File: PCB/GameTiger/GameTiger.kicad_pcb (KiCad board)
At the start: 2 copper layers, 5 parts, among them U1 RP2040, U2 NCP1117-3.3_SOT223, U3 W25Q128JVS, U4 PAM8302A, U5 PCF8575DB

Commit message: PCB Schematic for V2.0 is completed
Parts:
- added D1: MBR0540, Diode_SMD:D_SOD-123, F.Cu at (156.7, 83.3)
- U2: value NCP1117-3.3_SOT223 -> MCP73831-2-OT; footprint Package_TO_SOT_SMD:SOT-223-3_TabPin2 -> Package_TO_SOT_SMD:SOT-23-5
- U5: value PCF8575DB -> AP2112K-3.3; footprint PCF8575:pcf8575dbr -> Package_TO_SOT_SMD:SOT-23-5
- moved U4 21.3 mm to (109.6, 96.3)
- moved U5 7.34 mm to (144.2, 68.0)
- turned U2 to -90 degrees
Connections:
- net Net-(J2-CLK) renamed MicroSD_CLK
- net Net-(J2-CMD) renamed MicroSD_MOSI
- net Net-(J2-DAT0) renamed MicroSD_MISO
- net Net-(J2-DAT3/CD) renamed MicroSD_CS
- net Net-(U1-QSPI_SCLK) renamed Flash_QSPI_CLK
- net Net-(U1-QSPI_SD0) renamed Flash_QSPI_SD0
- net Net-(U1-QSPI_SD1) renamed Flash_QSPI_SD1
- net Net-(U1-QSPI_SD2) renamed Flash_QSPI_SD2
- net Net-(U1-QSPI_SD3) renamed Flash_QSPI_SD3
- net Net-(U1-QSPI_SS) renamed Flash_QSPI_SS
- net Net-(U1-XIN) renamed Crystal_XIN
- U1 pad 11: unconnected-(U1-GPIO8-Pad11) -> LCD_DC
- U1 pad 12: unconnected-(U1-GPIO9-Pad12) -> LCD_CS
- U1 pad 13: unconnected-(U1-GPIO10-Pad13) -> LCD_CLK
- U1 pad 14: unconnected-(U1-GPIO11-Pad14) -> LCD_DATA
- U1 pad 15: unconnected-(U1-GPIO12-Pad15) -> KYBD_UP
- U1 pad 16: unconnected-(U1-GPIO13-Pad16) -> KYBD_DOWN
- U1 pad 17: unconnected-(U1-GPIO14-Pad17) -> KYBD_LEFT
- U1 pad 18: unconnected-(U1-GPIO15-Pad18) -> KYBD_RIGHT
- U1 pad 2: Net-(U1-GPIO0) -> unconnected-(U1-GPIO0-Pad2)
- U1 pad 26: unconnected-(U1-RUN-Pad26) -> Net-(U1-RUN)
- U1 pad 27: unconnected-(U1-GPIO16-Pad27) -> KYBD_A
- U1 pad 28: unconnected-(U1-GPIO17-Pad28) -> KYBD_B
- U1 pad 29: unconnected-(U1-GPIO18-Pad29) -> KYBD_SELECT
- U1 pad 30: unconnected-(U1-GPIO19-Pad30) -> KYBD_START
- U1 pad 31: Net-(U1-GPIO20) -> Audio_PWM
- U1 pad 32: Net-(U1-GPIO21) -> MicroSD_DET
- U1 pad 9: unconnected-(U1-GPIO7-Pad9) -> LCD_RESET
- U2 pad 1: GND -> Net-(U2-STAT)
- U2 pad 2: +3.3V -> GND
- U2 pad 3: VBUS -> VBAT
- U4 pad 6: +3.3V -> VBAT
- U5 pad 1: unconnected-(U5-*INT-Pad1) -> Net-(D1-K)
- U5 pad 2: unconnected-(U5-A1-Pad2) -> GND
- U5 pad 3: unconnected-(U5-A2-Pad3) -> Net-(U5-EN)
- U5 pad 5: unconnected-(U5-P01-Pad5) -> +3.3V

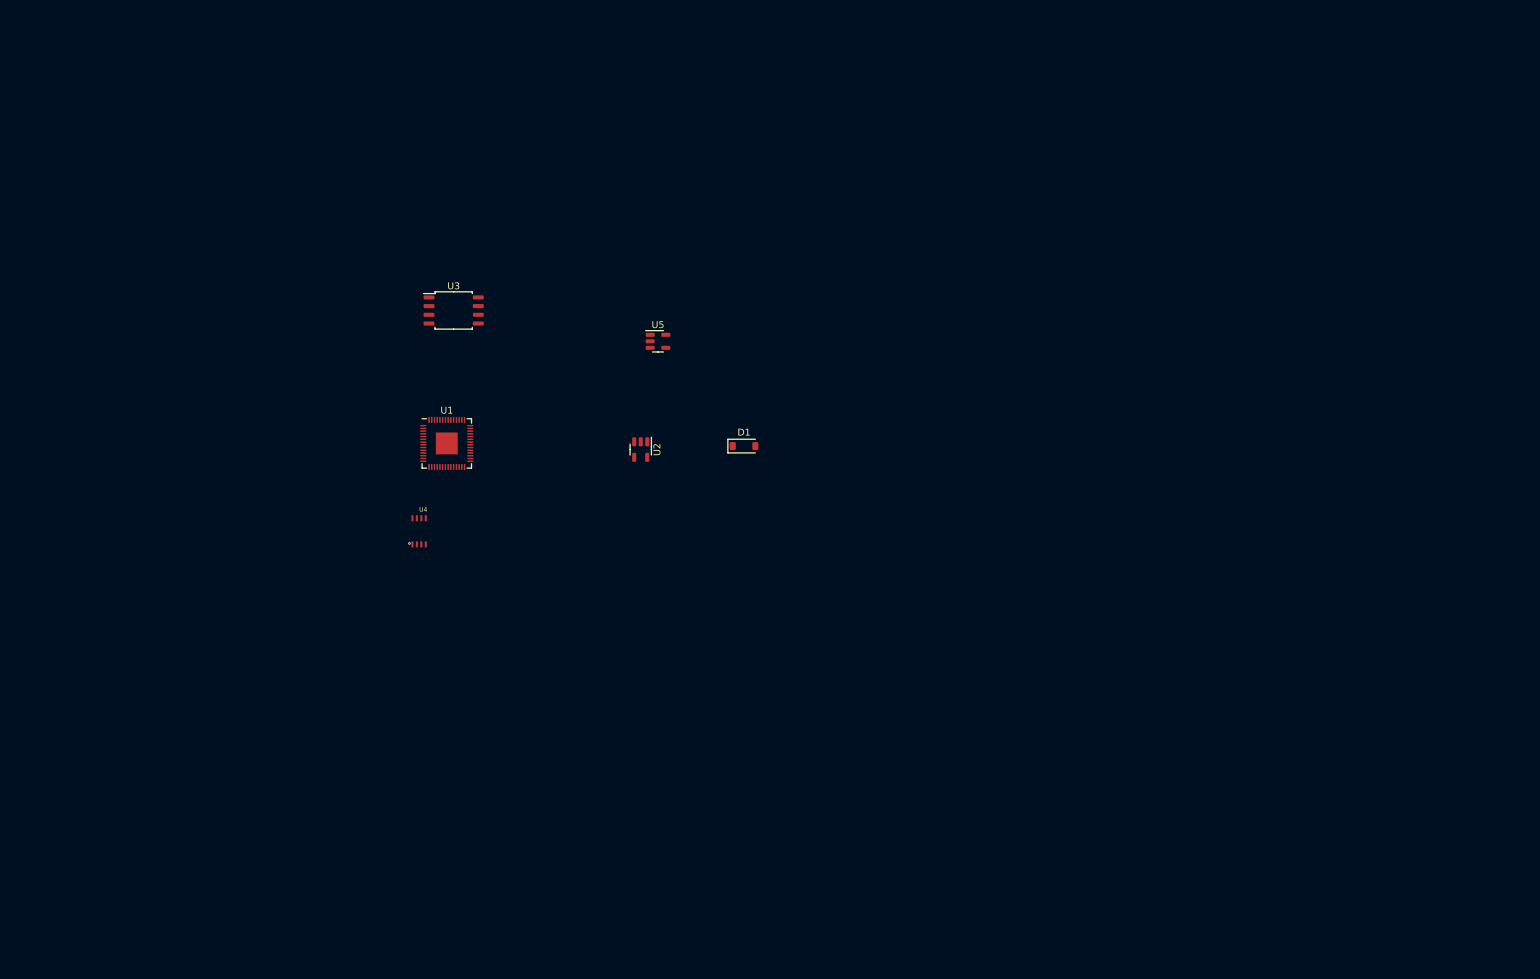
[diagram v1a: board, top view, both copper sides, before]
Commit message: Updated Schematics to correct footprints
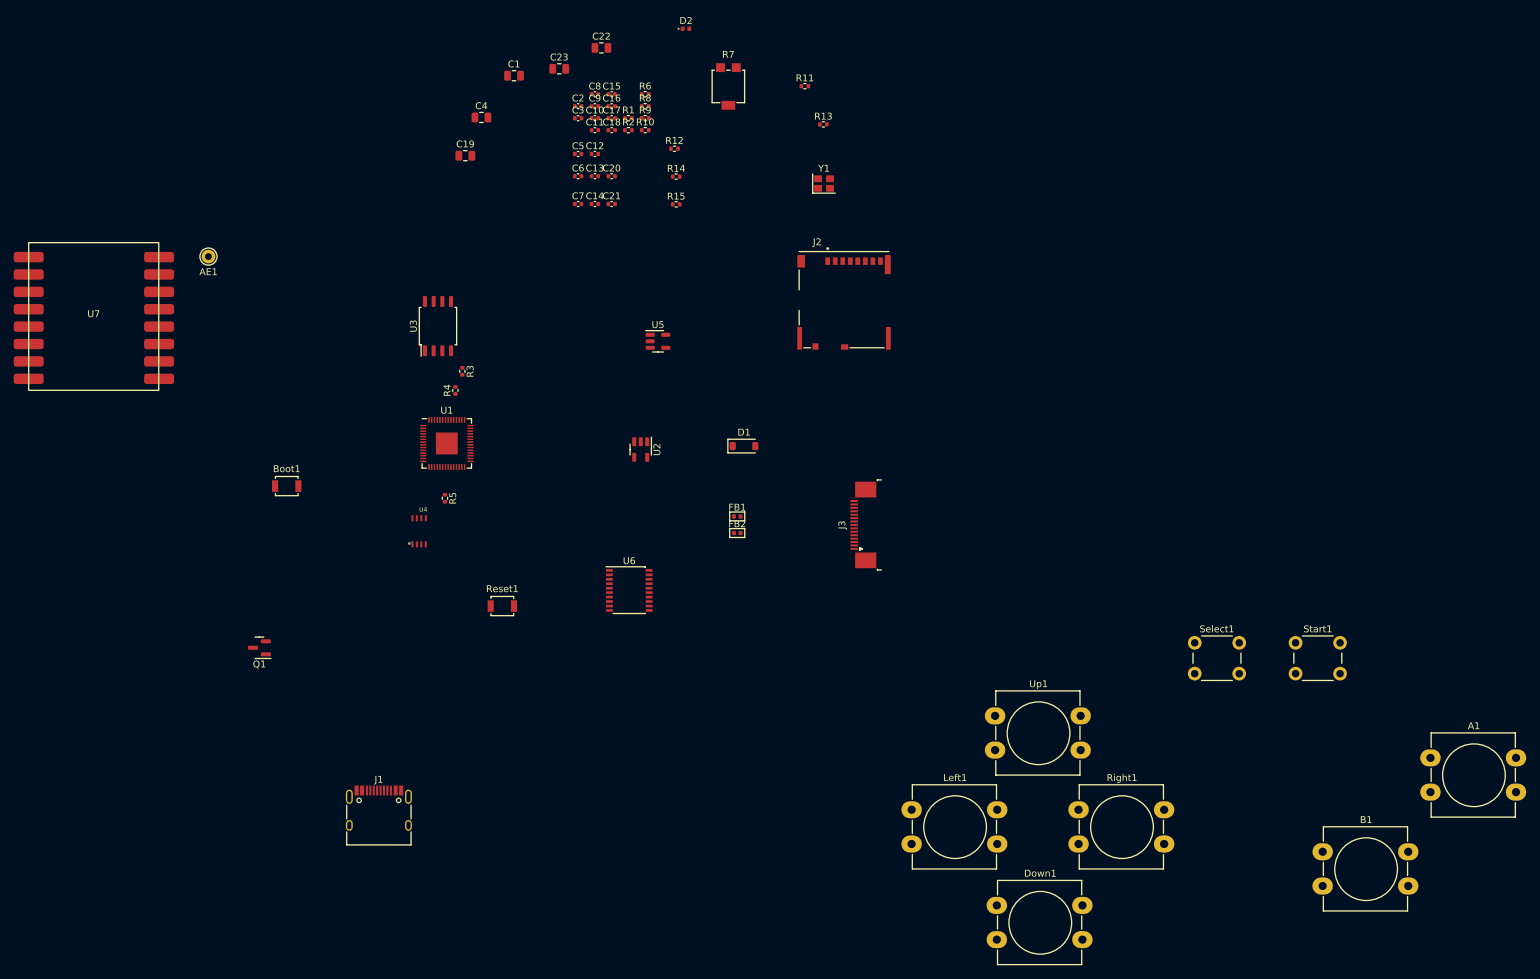
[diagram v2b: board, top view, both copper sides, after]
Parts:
- added A1: SW_Push, Button_Switch_THT:SW_PUSH-12mm_Wuerth-430476085716, F.Cu at (257.0, 128.9)
- added AE1: Antenna, Connector_Pin:Pin_D1.0mm_L10.0mm, F.Cu at (78.5, 55.6)
- added B1: SW_Push, Button_Switch_THT:SW_PUSH-12mm_Wuerth-430476085716, F.Cu at (241.2, 142.6)
- added Boot1: SW_Push, Button_Switch_SMD:SW_SPST_B3U-1000P, F.Cu at (89.9, 89.2)
- added C1: 10μF, Capacitor_SMD:C_0805_2012Metric, F.Cu at (123.1, 29.2)
- added C10: 100nF, Capacitor_SMD:C_0402_1005Metric, F.Cu at (134.9, 35.4)
- added C11: 100nF, Capacitor_SMD:C_0402_1005Metric, F.Cu at (134.9, 37.2)
- added C12: 100nF, Capacitor_SMD:C_0402_1005Metric, F.Cu at (134.9, 40.6)
- added C13: 100nF, Capacitor_SMD:C_0402_1005Metric, F.Cu at (134.9, 43.9)
- added C14: 100nF, Capacitor_SMD:C_0402_1005Metric, F.Cu at (134.9, 48.0)
- added C15: 100nF, Capacitor_SMD:C_0402_1005Metric, F.Cu at (137.4, 31.9)
- added C16: 100nF, Capacitor_SMD:C_0402_1005Metric, F.Cu at (137.4, 33.7)
- added C17: 1μF, Capacitor_SMD:C_0402_1005Metric, F.Cu at (137.4, 35.4)
- added C18: 1μF, Capacitor_SMD:C_0402_1005Metric, F.Cu at (137.4, 37.2)
- added C19: 10μF, Capacitor_SMD:C_0805_2012Metric, F.Cu at (116.0, 40.9)
- added C2: 27pF, Capacitor_SMD:C_0402_1005Metric, F.Cu at (132.5, 33.7)
- added C20: 220pF, Capacitor_SMD:C_0402_1005Metric, F.Cu at (137.4, 43.9)
- added C21: 220pF, Capacitor_SMD:C_0402_1005Metric, F.Cu at (137.4, 48.0)
- added C22: 10μF, Capacitor_SMD:C_0805_2012Metric, F.Cu at (135.9, 25.1)
- added C23: 10μF, Capacitor_SMD:C_0805_2012Metric, F.Cu at (129.7, 28.2)
- added C3: 27pF, Capacitor_SMD:C_0402_1005Metric, F.Cu at (132.5, 35.4)
- added C4: 10μF, Capacitor_SMD:C_0805_2012Metric, F.Cu at (118.4, 35.3)
- added C5: 100nF, Capacitor_SMD:C_0402_1005Metric, F.Cu at (132.5, 40.6)
- added C6: 1μF, Capacitor_SMD:C_0402_1005Metric, F.Cu at (132.5, 43.9)
- added C7: 100nF, Capacitor_SMD:C_0402_1005Metric, F.Cu at (132.5, 48.0)
- added C8: 100nF, Capacitor_SMD:C_0402_1005Metric, F.Cu at (134.9, 31.9)
- added C9: 1μF, Capacitor_SMD:C_0402_1005Metric, F.Cu at (134.9, 33.7)
- added D2: Orange, LED_SMD:LED_0402_1005Metric, F.Cu at (148.2, 22.4)
- added Down1: SW_Push, Button_Switch_THT:SW_PUSH-12mm_Wuerth-430476085716, F.Cu at (193.6, 150.4)
- added FB1: FerriteBead_Small, PCM_Ferrite_SMD_AKL:Ferrite_0402_1005Metric, F.Cu at (155.7, 93.6)
- added FB2: FerriteBead_Small, PCM_Ferrite_SMD_AKL:Ferrite_0402_1005Metric, F.Cu at (155.7, 96.0)
- added J1: USB_C_Receptacle_USB2.0, Connector_USB:USB_C_Receptacle_HRO_TYPE-C-31-M-12, F.Cu at (103.4, 137.7)
- added J2: 503398-1892, 503398-1892:MOLEX_503398-1892, F.Cu at (171.3, 61.9)
- added J3: LCD Display, Connector_FFC-FPC:TE_1-1734839-5_1x15-1MP_P0.5mm_Horizontal, F.Cu at (174.1, 94.8)
- added Left1: SW_Push, Button_Switch_THT:SW_PUSH-12mm_Wuerth-430476085716, F.Cu at (181.2, 136.4)
- added Q1: DMG3415, Package_TO_SOT_SMD:SOT-23, F.Cu at (85.9, 112.8)
- added R1: 1kΩ, Resistor_SMD:R_0402_1005Metric, F.Cu at (139.8, 35.4)
- added R10: 10KΩ, Resistor_SMD:R_0402_1005Metric, F.Cu at (142.3, 37.2)
- added R11: 5.1KΩ, Resistor_SMD:R_0402_1005Metric, F.Cu at (165.6, 30.7)
- added R12: 10KΩ, Resistor_SMD:R_0402_1005Metric, F.Cu at (146.6, 39.9)
- added R13: 10KΩ, Resistor_SMD:R_0402_1005Metric, F.Cu at (168.3, 36.3)
- added R14: 5.1KΩ, Resistor_SMD:R_0402_1005Metric, F.Cu at (146.8, 43.9)
- added R15: 5.1KΩ, Resistor_SMD:R_0402_1005Metric, F.Cu at (146.8, 48.0)
- added R2: 10kΩ, Resistor_SMD:R_0402_1005Metric, F.Cu at (139.8, 37.2)
- added R3: 27Ω, Resistor_SMD:R_0402_1005Metric, F.Cu at (115.6, 72.4)
- added R4: 27Ω, Resistor_SMD:R_0402_1005Metric, F.Cu at (114.6, 75.2)
- added R5: 1kΩ, Resistor_SMD:R_0402_1005Metric, F.Cu at (113.0, 90.9)
- added R6: 10KΩ, Resistor_SMD:R_0402_1005Metric, F.Cu at (142.3, 31.9)
- added R7: 10KΩ, Potentiometer_SMD:Potentiometer_Bourns_3314G_Vertical, F.Cu at (154.4, 30.8)
- added R8: 100Ω, Resistor_SMD:R_0402_1005Metric, F.Cu at (142.3, 33.7)
- added R9: 100Ω, Resistor_SMD:R_0402_1005Metric, F.Cu at (142.3, 35.4)
- added Reset1: SW_Push, Button_Switch_SMD:SW_SPST_B3U-1000P, F.Cu at (121.4, 106.7)
- added Right1: SW_Push, Button_Switch_THT:SW_PUSH-12mm_Wuerth-430476085716, F.Cu at (205.6, 136.4)
- added Select1: SW_Push, Button_Switch_THT:SW_PUSH_6mm, F.Cu at (222.6, 112.0)
- added Start1: SW_Push, Button_Switch_THT:SW_PUSH_6mm, F.Cu at (237.3, 112.0)
- added U6: PCF8574TS, Package_SO:SSOP-20_4.4x6.5mm_P0.65mm, F.Cu at (140.0, 104.4)
- added U7: ~, Waveshare:Core SX1262, F.Cu at (61.7, 64.5)
- added Up1: SW_Push, Button_Switch_THT:SW_PUSH-12mm_Wuerth-430476085716, F.Cu at (193.4, 122.7)
- added Y1: ABLS-12MHZ-B4-T, Crystal:Crystal_SMD_2520-4Pin_2.5x2.0mm, F.Cu at (168.4, 45.0)
- moved U3 3.23 mm to (112.0, 65.8), turned to 90 degrees
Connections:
- U1 pad 11: LCD_DC -> SX1262_MISO
- U1 pad 12: LCD_CS -> SX1262_CS
- U1 pad 13: LCD_CLK -> SX1262_CLK
- U1 pad 14: LCD_DATA -> SX1262_MOSI
- U1 pad 15: KYBD_UP -> LCD_DC
- U1 pad 16: KYBD_DOWN -> LCD_CS
- U1 pad 17: KYBD_LEFT -> LCD_CLK
- U1 pad 18: KYBD_RIGHT -> LCD_DATA
- U1 pad 27: KYBD_A -> LCD_RESET
- U1 pad 28: KYBD_B -> Audio_PWM
- U1 pad 29: KYBD_SELECT -> KYBD_SDA
- U1 pad 30: KYBD_START -> KYBD_SCL
- U1 pad 31: Audio_PWM -> KYBD_INT
- U1 pad 32: MicroSD_DET -> MicroSD_DETECT
- U1 pad 7: unconnected-(U1-GPIO5-Pad7) -> SX1262_DIO1
- U1 pad 8: unconnected-(U1-GPIO6-Pad8) -> SX1262_RESET
- U1 pad 9: LCD_RESET -> SX1262_BUSY

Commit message: PCB layout completed with all tracks and connections
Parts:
- C1, C10, C11, C12, C13, C14, C15, C16, C17, C18, C19, C2, C20, C21, C22, C23, C3, C4, C5, C6, C7, C8, C9, D1, D2, FB1, FB2, J1, J2, J3, Q1, R1, R10, R11, R12, R13, R14, R15, R2, R3, R4, R5, R6, R7, R8, R9, U1, U2, U3, U4, U5, U7, Y1: moved to B.Cu
- moved A1 159.3 mm to (100.2, 101.1)
- moved B1 152.0 mm to (91.2, 118.4)
- moved Select1 148.8 mm to (75.5, 89.7)
- moved Start1 148.8 mm to (90.2, 89.7)
- moved Right1 144.7 mm to (63.7, 108.0)
- moved Up1 144.7 mm to (51.5, 94.3)
- moved Down1 144.7 mm to (51.8, 122.0)
- moved Left1 144.7 mm to (39.3, 108.0)
- moved R11 127.0 mm to (82.8, 127.0), turned to -90 degrees
- moved R13 119.7 mm to (83.1, 120.4)
- moved D2 118.9 mm to (81.0, 120.4), turned to 180 degrees
- moved C23 113.6 mm to (88.1, 133.9), turned to 90 degrees
- moved R14 110.8 mm to (74.4, 127.8), turned to 90 degrees
- moved R10 107.9 mm to (80.3, 125.5)
- moved Reset1 105.4 mm to (46.5, 32.5), turned to 180 degrees
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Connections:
- U1 pad 11: SX1262_MISO -> unconnected-(U1-GPIO8-Pad11)
- U1 pad 12: SX1262_CS -> unconnected-(U1-GPIO9-Pad12)
- U1 pad 13: SX1262_CLK -> unconnected-(U1-GPIO10-Pad13)
- U1 pad 14: SX1262_MOSI -> SX1262_DIO1
- U1 pad 15: LCD_DC -> SX1262_BUSY
- U1 pad 16: LCD_CS -> SX1262_MISO
- U1 pad 17: LCD_CLK -> SX1262_CS
- U1 pad 18: LCD_DATA -> SX1262_CLK
- U1 pad 2: unconnected-(U1-GPIO0-Pad2) -> LCD_DC
- U1 pad 27: LCD_RESET -> SX1262_MOSI
- U1 pad 28: Audio_PWM -> SX1262_RESET
- U1 pad 3: unconnected-(U1-GPIO1-Pad3) -> LCD_CS
- U1 pad 4: unconnected-(U1-GPIO2-Pad4) -> LCD_CLK
- U1 pad 5: unconnected-(U1-GPIO3-Pad5) -> LCD_DATA
- U1 pad 6: unconnected-(U1-GPIO4-Pad6) -> LCD_RESET
- U1 pad 7: SX1262_DIO1 -> unconnected-(U1-GPIO5-Pad7)
- U1 pad 8: SX1262_RESET -> Audio_PWM
- U1 pad 9: SX1262_BUSY -> unconnected-(U1-GPIO7-Pad9)
- U6 pad 11: KYBD_DOWN -> KYBD_LEFT
- U6 pad 12: KYBD_LEFT -> KYBD_RIGHT
- U6 pad 14: KYBD_RIGHT -> KYBD_DOWN
- U6 pad 16: KYBD_A -> KYBD_B
- U6 pad 17: KYBD_B -> KYBD_A
- U6 pad 19: KYBD_SELECT -> KYBD_START
- U6 pad 20: KYBD_START -> KYBD_SELECT
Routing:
- net GND: track 0.00 -> 150.9 mm, vias 0 -> 20
- net POWER_USB_DM: track 0.00 -> 95.4 mm, vias 0 -> 2
- net POWER_USB_DP: track 0.00 -> 91.5 mm, vias 0 -> 2
- net +3.3V: track 0.00 -> 86.2 mm, vias 0 -> 7
- net SX1262_CLK: track 0.00 -> 80.3 mm
- net SX1262_CS: track 0.00 -> 70.2 mm
- net VBAT: track 0.00 -> 65.7 mm
- net SX1262_MISO: track 0.00 -> 65.5 mm
- net Audio_PWM: track 0.00 -> 57.2 mm
- net KYBD_SCL: track 0.00 -> 57.0 mm, vias 0 -> 1
- net KYBD_SDA: track 0.00 -> 56.9 mm, vias 0 -> 1
- net KYBD_INT: track 0.00 -> 56.9 mm, vias 0 -> 1
- net SX1262_DIO1: track 0.00 -> 56.7 mm, vias 0 -> 2
- net KYBD_LEFT: track 0.00 -> 56.7 mm, vias 0 -> 1
- net Net-(U1-RUN): track 0.00 -> 53.6 mm, vias 0 -> 1
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- added copper zone on F.Cu, net +3.3V
- added copper zone on B.Cu, net GND
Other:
- board outline added: 86.4 x 107.2 mm

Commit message: Added more details on the PCB components
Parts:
- added H1: MountingHole, MountingHole:MountingHole_2.2mm_M2, F.Cu at (40.6, 129.5)
- added H2: MountingHole, MountingHole:MountingHole_2.2mm_M2, F.Cu at (111.8, 129.5)
- added H3: MountingHole, MountingHole:MountingHole_2.2mm_M2, F.Cu at (111.8, 37.6)
- added H4: MountingHole, MountingHole:MountingHole_2.2mm_M2, F.Cu at (40.6, 37.6)
- added J4: Speaker, Connector_Wire:SolderWire-0.5sqmm_1x02_P4.6mm_D0.9mm_OD2.1mm, F.Cu at (114.0, 78.3)
- added Power1: SW_Push, Button_Switch_SMD:SW_SPDT_CK-JS102011SAQN, F.Cu at (117.1, 54.4)
- added R16: 10KΩ, Resistor_SMD:R_0402_1005Metric, B.Cu at (62.2, 63.5)
- added X1: ~, Connector_JST:JST_PH_S2B-PH-SM4-TB_1x02-1MP_P2.00mm_Horizontal, B.Cu at (43.0, 90.5)
- C1, C19, C22, C23, C4: value 10μF -> 10uF
- C17, C18, C6, C9: value 1μF -> 1uF
- C20, C21: footprint Capacitor_SMD:C_0402_1005Metric -> Capacitor_SMD:C_0805_2012Metric
- FB1, FB2: footprint PCM_Ferrite_SMD_AKL:Ferrite_0402_1005Metric -> PCM_Ferrite_SMD_AKL:Ferrite_0805_2012Metric
- R7: footprint Potentiometer_SMD:Potentiometer_Bourns_3314G_Vertical -> Potentiometer_SMD:Potentiometer_Bourns_TC33X_Vertical
- U3: value W25Q128JVS -> W25Q128JVSIQ
- moved U7 14.7 mm to (47.0, 62.5)
- moved AE1 13.7 mm to (38.1, 79.5)
- moved C20 1.78 mm to (107.2, 84.6)
- moved C21 1.78 mm to (103.9, 84.6)
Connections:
- net Net-(U5-EN) renamed EN
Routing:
- net EN: track 2.35 -> 98.2 mm, vias 0 -> 1
- net VBAT: track 65.7 -> 137.6 mm
- net Net-(J4-Pin_2): track 1.32 -> 21.7 mm, vias 0 -> 1
- net SX1262_MISO: track 65.5 -> 49.3 mm
- net Net-(J4-Pin_1): track 1.30 -> 16.2 mm, vias 0 -> 1
- net SX1262_DIO1: track 56.7 -> 71.5 mm
- net SX1262_CS: track 70.2 -> 57.2 mm
- net SX1262_CLK: track 80.3 -> 68.1 mm
- net SX1262_BUSY: track 53.5 -> 42.4 mm
- net SX1262_MOSI: track 30.8 -> 35.6 mm
- net Net-(U1-RUN): track 53.6 -> 57.9 mm
- net SX1262_RESET: track 25.6 -> 29.4 mm
- net GND: track 150.9 -> 153.3 mm, vias 20 -> 21
- net +3.3V: track 86.2 -> 87.3 mm, vias 7 -> 8
- net Net-(AE1-A): track 8.41 -> 7.50 mm
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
